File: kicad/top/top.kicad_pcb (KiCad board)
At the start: 2 copper layers, 62 x 119.5 mm, 32 parts, among them J1 OLED_128x64, J2 Conn_01x15, SW1 SW_SPDT, SW2 RotaryEncoder_Switch

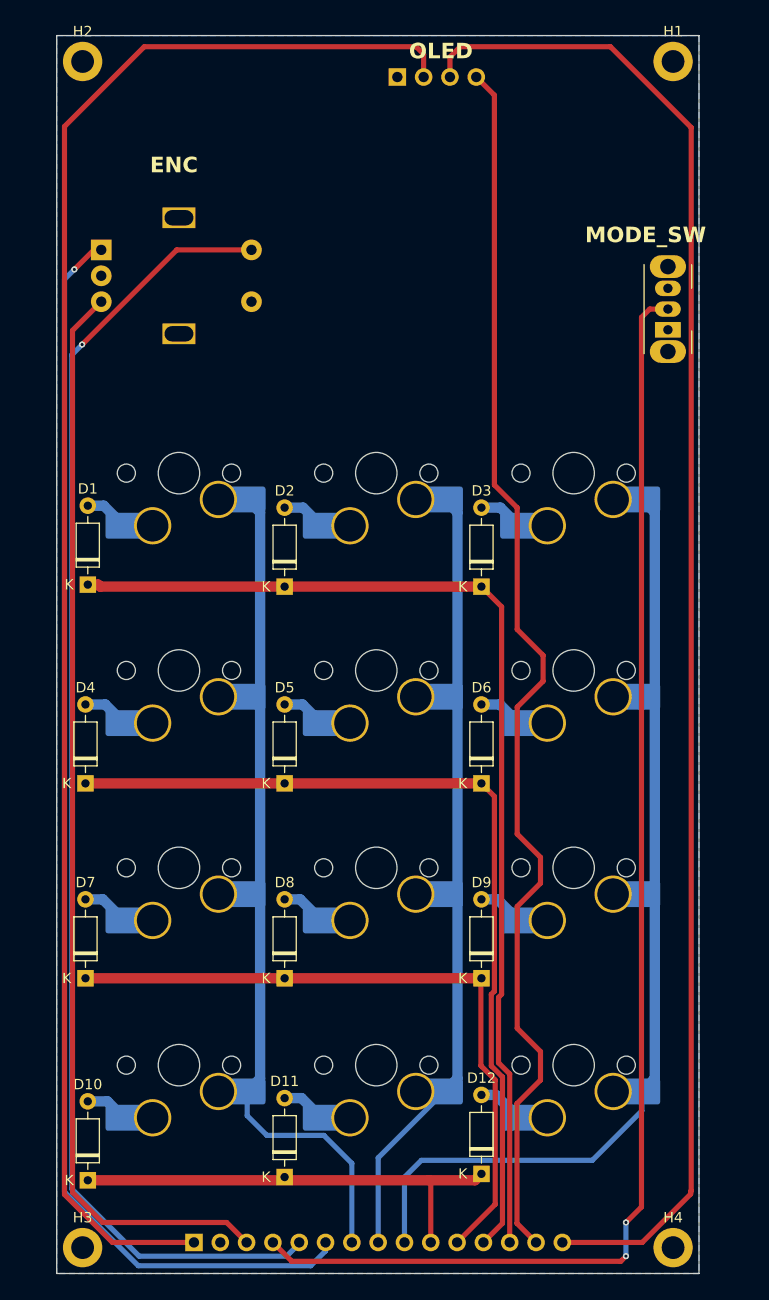
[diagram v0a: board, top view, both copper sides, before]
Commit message: added cutout for battery jst connector on bottom pcb
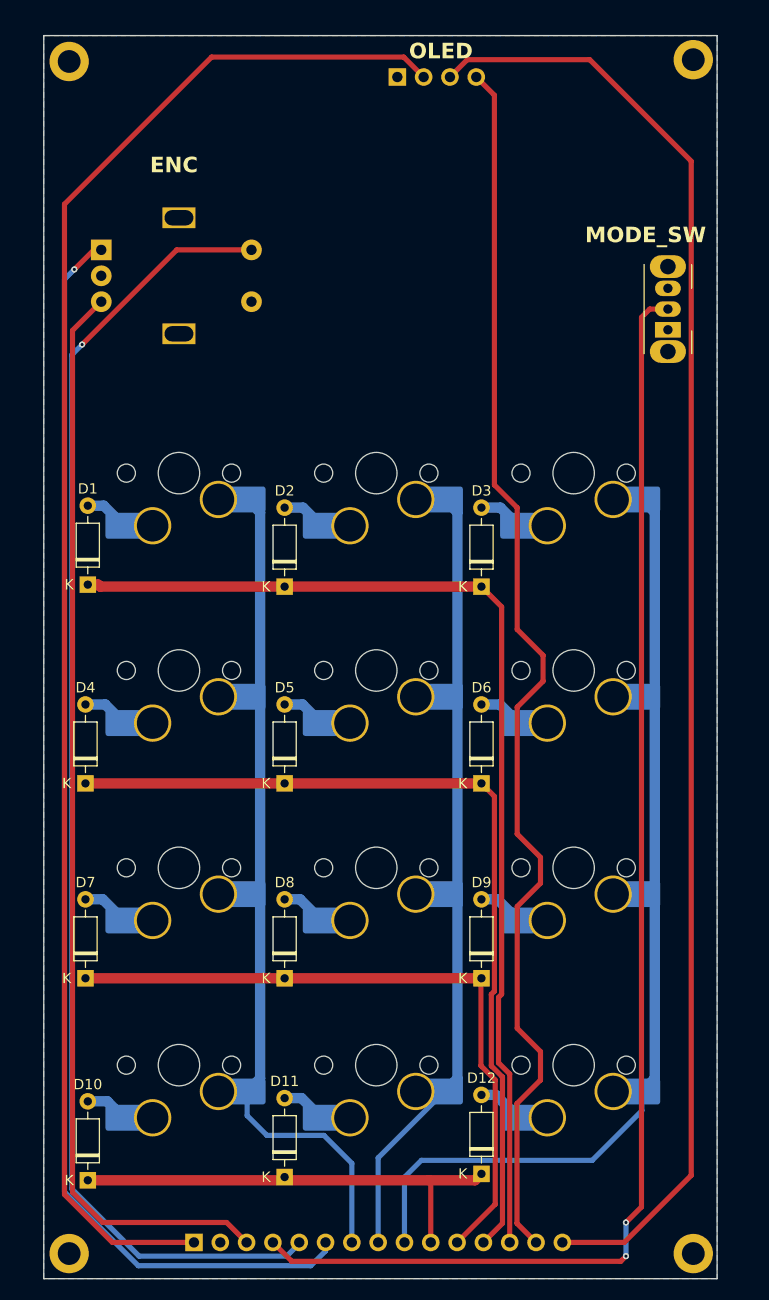
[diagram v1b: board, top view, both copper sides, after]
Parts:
- moved H4 2.03 mm to (75.5, 137.5)
- moved H1 1.96 mm to (75.5, 22.2)
- moved H3 1.42 mm to (15.2, 137.5)
- moved H2 1.30 mm to (15.2, 22.4)
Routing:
- net +3.3V: track 157.9 -> 151.4 mm
- net OLED_SCL: track 146.2 -> 141.1 mm
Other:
- board size 62 x 119.5 mm -> 65 x 120 mm
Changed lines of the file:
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@@
 	(footprint "MountingHole:MountingHole_2.2mm_M2_DIN965_Pad"
 		(layer "F.Cu")
-		(at 16.5475 22.425)
+		(at 15.2475 22.425)
 		(descr "Mounting Hole 2.2mm, M2, DIN965")
 		(tags "mounting hole 2.2mm m2 din965")
@@
 			(at 0 -2.9 0)
 			(layer "F.SilkS")
+			(hide yes)
 			(effects
 				(font
@@
 			(at 0 2.9 0)
 			(layer "F.Fab")
+			(hide yes)
 			(effects
 				(font
@@
 	(footprint "MountingHole:MountingHole_2.2mm_M2_DIN965_Pad"
 		(layer "F.Cu")
-		(at 73.5475 22.425)
+		(at 75.4975 22.25)
 		(descr "Mounting Hole 2.2mm, M2, DIN965")
 		(tags "mounting hole 2.2mm m2 din965")
@@
 			(at 0 -2.9 0)
 			(layer "F.SilkS")
+			(hide yes)
 			(effects
 				(font
@@
 			(at 0 2.9 0)
 			(layer "F.Fab")
+			(hide yes)
 			(effects
 				(font
@@
 	(footprint "MountingHole:MountingHole_2.2mm_M2_DIN965_Pad"
 		(layer "F.Cu")
-		(at 16.5475 136.925)
+		(at 15.2475 137.5)
 		(descr "Mounting Hole 2.2mm, M2, DIN965")
 		(tags "mounting hole 2.2mm m2 din965")
@@
 			(at 0 -2.9 0)
 			(layer "F.SilkS")
+			(hide yes)
 			(effects
 				(font
@@
 			(at 0 2.9 0)
 			(layer "F.Fab")
+			(hide yes)
 			(effects
 				(font
@@
 	(footprint "MountingHole:MountingHole_2.2mm_M2_DIN965_Pad"
 		(layer "F.Cu")
-		(at 73.5475 136.925)
+		(at 75.4975 137.5)
 		(descr "Mounting Hole 2.2mm, M2, DIN965")
 		(tags "mounting hole 2.2mm m2 din965")
@@
 			(at 0 -2.9 0)
 			(layer "F.SilkS")
+			(hide yes)
 			(effects
 				(font
@@
 			(at 0 2.9 0)
 			(layer "F.Fab")
+			(hide yes)
 			(effects
 				(font
@@
 	)
 	(gr_rect
-		(start 14.0475 19.925)
-		(end 76.0475 139.425)
+		(start 12.7975 19.925)
+		(end 77.7975 139.925)
 		(stroke
 			(width 0.05)
@@
 	)
 	(segment
-		(start 75.2475 131.5)
-		(end 75.2975 131.45)
+		(start 75.2975 32.05)
+		(end 65.4975 22.25)
 		(width 0.5)
 		(layer "F.Cu")
@@
 	)
 	(segment
-		(start 52.0075 21.99)
+		(start 53.6825 22.25)
 		(end 52.0075 23.925)
 		(width 0.5)
@@
 	)
 	(segment
-		(start 70.5725 136.425)
-		(end 75.2475 131.75)
-		(width 0.5)
-		(layer "F.Cu")
-		(net 25)
-	)
-	(segment
-		(start 62.8575 136.425)
-		(end 70.5725 136.425)
+		(start 75.2975 129.95)
+		(end 75.2975 32.05)
 		(width 0.5)
 		(layer "F.Cu")
@@
 	)
 	(segment
-		(start 75.2975 28.8)
-		(end 67.4975 21)
+		(start 68.8225 136.425)
+		(end 75.2975 129.95)
 		(width 0.5)
 		(layer "F.Cu")
@@
 	)
 	(segment
-		(start 52.9975 21)
-		(end 52.0075 21.99)
-		(width 0.5)
-		(layer "F.Cu")
-		(net 25)
-	)
-	(segment
-		(start 67.4975 21)
-		(end 52.9975 21)
-		(width 0.5)
-		(layer "F.Cu")
-		(net 25)
-	)
-	(segment
-		(start 75.2975 131.45)
-		(end 75.2975 28.8)
+		(start 62.8575 136.425)
+		(end 68.8225 136.425)
 		(width 0.5)
 		(layer "F.Cu")
@@
 	)
 	(segment
-		(start 75.2475 131.75)
-		(end 75.2475 131.5)
+		(start 65.4975 22.25)
+		(end 53.6825 22.25)
 		(width 0.5)
 		(layer "F.Cu")
@@
 	)
 	(segment
-		(start 22.4975 21)
-		(end 14.7975 28.7)
+		(start 19.4225 136.425)
+		(end 27.2975 136.425)
 		(width 0.5)
 		(layer "F.Cu")
@@
 	)
 	(segment
-		(start 19.4225 136.425)
-		(end 27.2975 136.425)
+		(start 14.7975 131.8)
+		(end 19.4225 136.425)
 		(width 0.5)
 		(layer "F.Cu")
@@
 	)
 	(segment
-		(start 14.7975 131.8)
-		(end 19.4225 136.425)
+		(start 49.4675 23.925)
+		(end 47.5425 22)
 		(width 0.5)
 		(layer "F.Cu")
@@
 	)
 	(segment
-		(start 14.7975 28.7)
+		(start 14.7975 36.2)
 		(end 14.7975 131.8)
 		(width 0.5)
@@
 	)
 	(segment
-		(start 48.7475 21)
-		(end 22.4975 21)
+		(start 49.4675 23.985)
+		(end 49.4675 23.925)
 		(width 0.5)
 		(layer "F.Cu")
@@
 	)
 	(segment
-		(start 49.4675 23.985)
-		(end 49.4675 21.72)
+		(start 28.9975 22)
+		(end 14.7975 36.2)
 		(width 0.5)
 		(layer "F.Cu")
@@
 	)
 	(segment
-		(start 49.4675 21.72)
-		(end 48.7475 21)
+		(start 47.5425 22)
+		(end 28.9975 22)
 		(width 0.5)
 		(layer "F.Cu")
@@
 		(layer "B.Cu")
 		(hatch edge 0.5)
-		(connect_pads yes
+		(connect_pads
 			(clearance 0.5)
 		)
@@
 		(polygon
 			(pts
-				(xy 76.0475 19.925) (xy 76.0475 139.425) (xy 14.0475 139.425) (xy 14.0475 19.925)
+				(xy 12.7975 19.925) (xy 77.7975 19.925) (xy 77.7975 139.925) (xy 12.7975 139.925)
 			)
 		)

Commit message: modify paths and file locations for portability, added mounting pins to encoder, changed symbol, footprint and 3d of switch to correlate to what im using
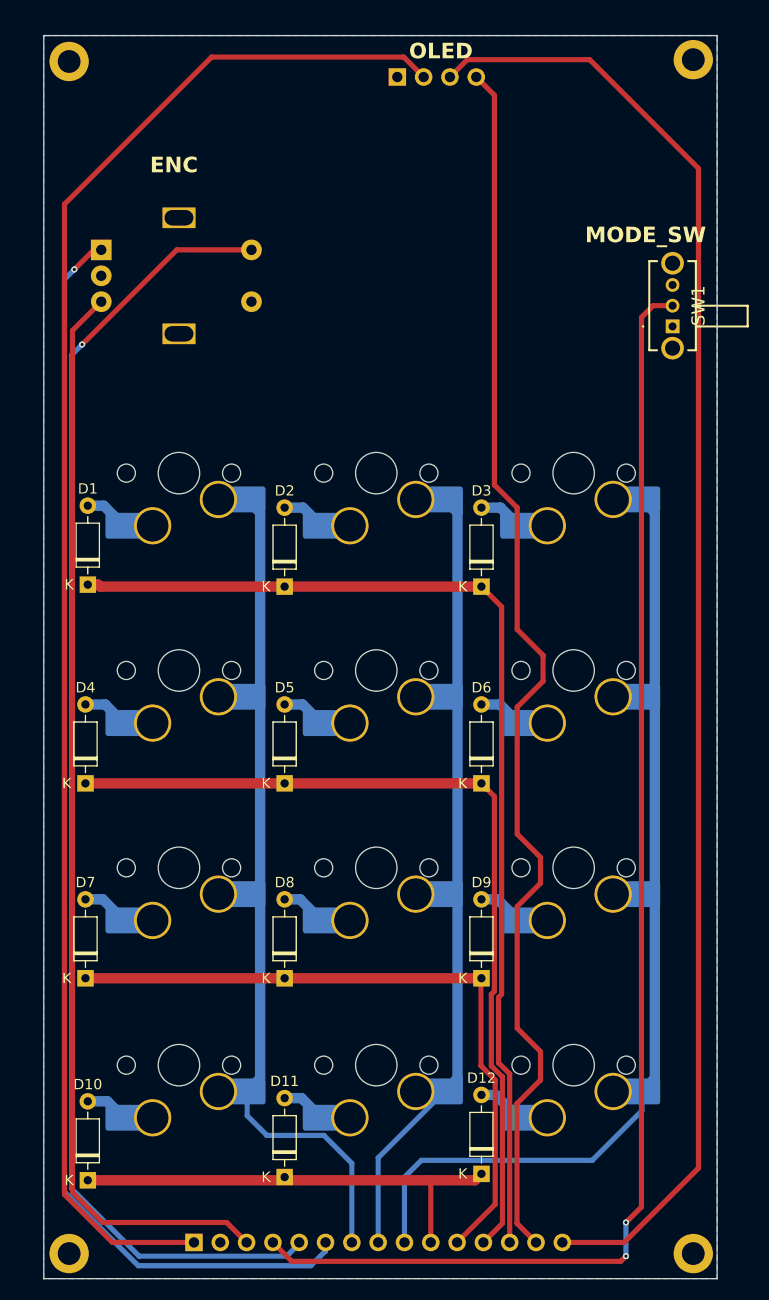
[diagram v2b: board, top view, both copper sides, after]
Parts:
- D1, D10, D11, D12, D2, D3, D4, D5, D6, D7, D8, D9: footprint Diode_THT:D_DO-35_SOD27_P7.62mm_Horizontal -> Project-Footprints:D_DO-35_SOD27_P7.62mm_Horizontal
- H1, H2, H3, H4: footprint MountingHole:MountingHole_2.2mm_M2_DIN965_Pad -> Project-Footprints:MountingHole_2.2mm_M2_DIN965_Pad
- J1: footprint ScottoKeebs_Components:OLED_128x64 -> Project-Footprints:OLED_128x64
- J2: footprint Connector_PinHeader_2.54mm:PinHeader_1x15_P2.54mm_Vertical -> Project-Footprints:PinHeader_1x15_P2.54mm_Vertical
- S1, S10, S11, S12, S2, S3, S4, S5, S6, S7, S8, S9: footprint ScottoKeebs_Scotto:MX_Hotswap_1.00u -> Project-Footprints:MX_Hotswap_1.00u
- SW1: value SW_SPDT -> SLW-864574-5A-RA-N-D; footprint Button_Switch_THT:SW_Slide_SPDT_Angled_CK_OS102011MA1Q -> Project-Footprints:SLW8645745ARAND
- SW2: footprint ScottoKeebs_Scotto:Encoder_EC11_MX -> Project-Footprints:Encoder_EC11_MX
- moved SW1 0.56 mm to (73.5, 48.0)
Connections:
- H1 pad 1: unconnected-(H1-Pad1) -> GND
- H2 pad 1: unconnected-(H2-Pad1) -> GND
- H3 pad 1: unconnected-(H3-Pad1) -> GND
- H4 pad 1: unconnected-(H4-Pad1) -> GND
- SW2 pad MP: (no net) -> unconnected-(SW2-PadMP)_1
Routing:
- net BT_SELECT: track 128.8 -> 129.4 mm
- net OLED_SCL: track 141.1 -> 141.6 mm

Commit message: finalised mounting hole and pins position, changed gpios
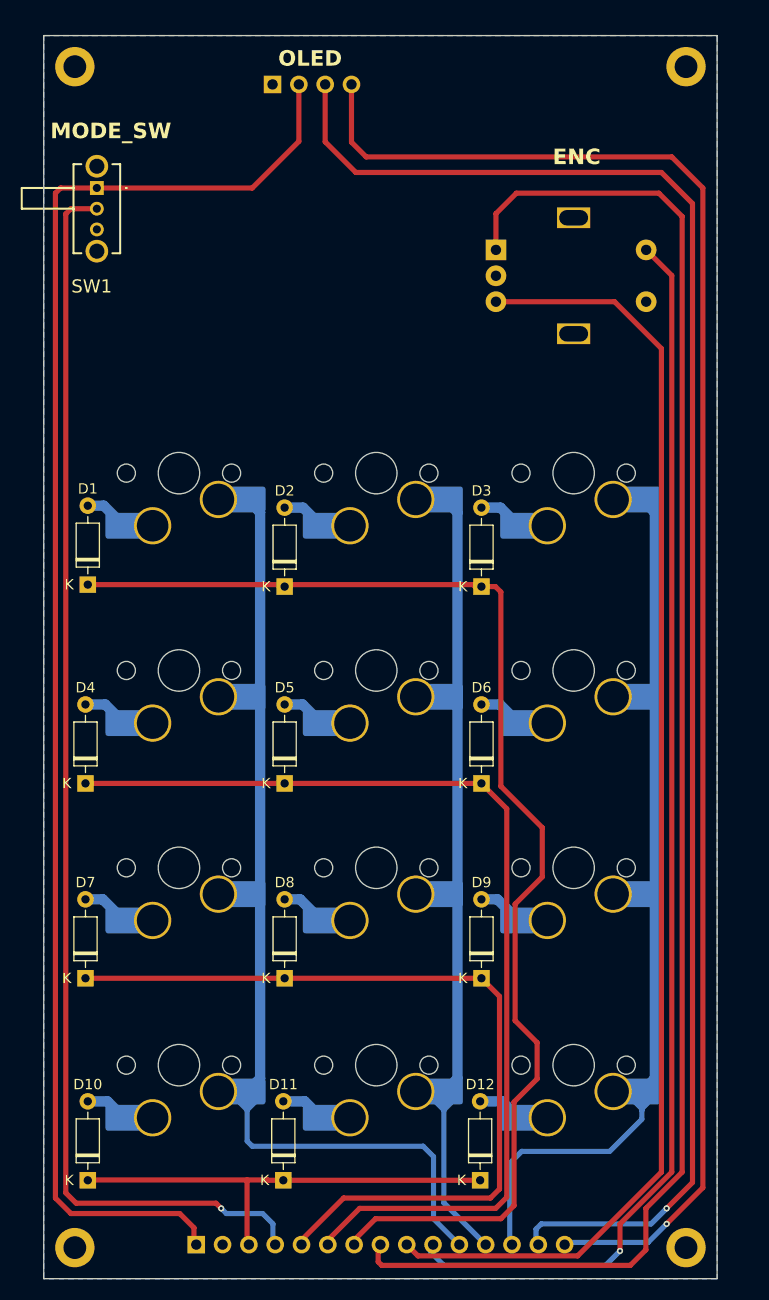
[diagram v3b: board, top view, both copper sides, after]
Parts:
- moved SW1 57.2 mm to (17.9, 34.6), turned to -90 degrees
- moved SW2 38.1 mm to (63.9, 43.1)
- moved J1 12.1 mm to (38.7, 24.6)
- moved H1 0.97 mm to (74.8, 22.9)
- moved H4 0.91 mm to (74.8, 136.9)
- moved H3 0.80 mm to (15.8, 136.9)
- moved H2 0.74 mm to (15.8, 22.9)
- moved D12 0.63 mm to (54.9, 130.4)
- moved D11 0.33 mm to (35.9, 130.4)
- moved J2 0.31 mm to (27.5, 136.6)
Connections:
- J2 pad 10: ROW3 -> ENC_SW
- J2 pad 11: ROW2 -> COL0
- J2 pad 12: ROW1 -> COL1
- J2 pad 13: ROW0 -> COL2
- J2 pad 14: OLED_SDA -> OLED_SCL
- J2 pad 15: OLED_SCL -> OLED_SDA
- J2 pad 3: ENC_DT -> ROW3
- J2 pad 5: ENC_SW -> ROW2
- J2 pad 6: ENC_CLK -> ROW1
- J2 pad 7: COL0 -> ROW0
- J2 pad 8: COL1 -> ENC_CLK
- J2 pad 9: COL2 -> ENC_DT
- SW1 pad 1: unconnected-(SW1-Pad1) -> +3.3V
- SW1 pad 4: unconnected-(SW1-MH1-Pad4) -> GND
- SW1 pad 5: unconnected-(SW1-MH2-Pad5) -> GND
- SW2 pad MP: unconnected-(SW2-PadMP)_1 -> GND
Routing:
- net OLED_SDA: track 120.7 -> 153.6 mm, vias 0 -> 1
- net ENC_CLK: track 122.4 -> 152.9 mm, vias 1 -> 0
- net ENC_DT: track 105.9 -> 126.0 mm
- net ROW0: track 102.8 -> 121.1 mm
- net COL0: track 80.2 -> 96.4 mm
- net ROW2: track 65.8 -> 80.8 mm
- net OLED_SCL: track 141.6 -> 156.2 mm, vias 0 -> 1
- net ROW1: track 84.4 -> 98.5 mm
- net BT_SELECT: track 129.4 -> 120.7 mm, vias 2 -> 1
- net +3.3V: track 151.4 -> 144.0 mm
- net ENC_SW: track 127.3 -> 120.0 mm
- net COL2: track 91.9 -> 87.4 mm
- net COL1: track 75.4 -> 77.2 mm
